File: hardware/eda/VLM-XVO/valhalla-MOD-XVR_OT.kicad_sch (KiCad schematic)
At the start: 35 parts, among them J1 OT+_Boiler, J2 GPIO, J3 OT+_Thermostat, J4 BUS, Q1 Q_PNP, Q2 Q_PNP, Q3 Q_PNP, Q4 Q_PNP, Q5 Q_NPN, Q6 Q_NPN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

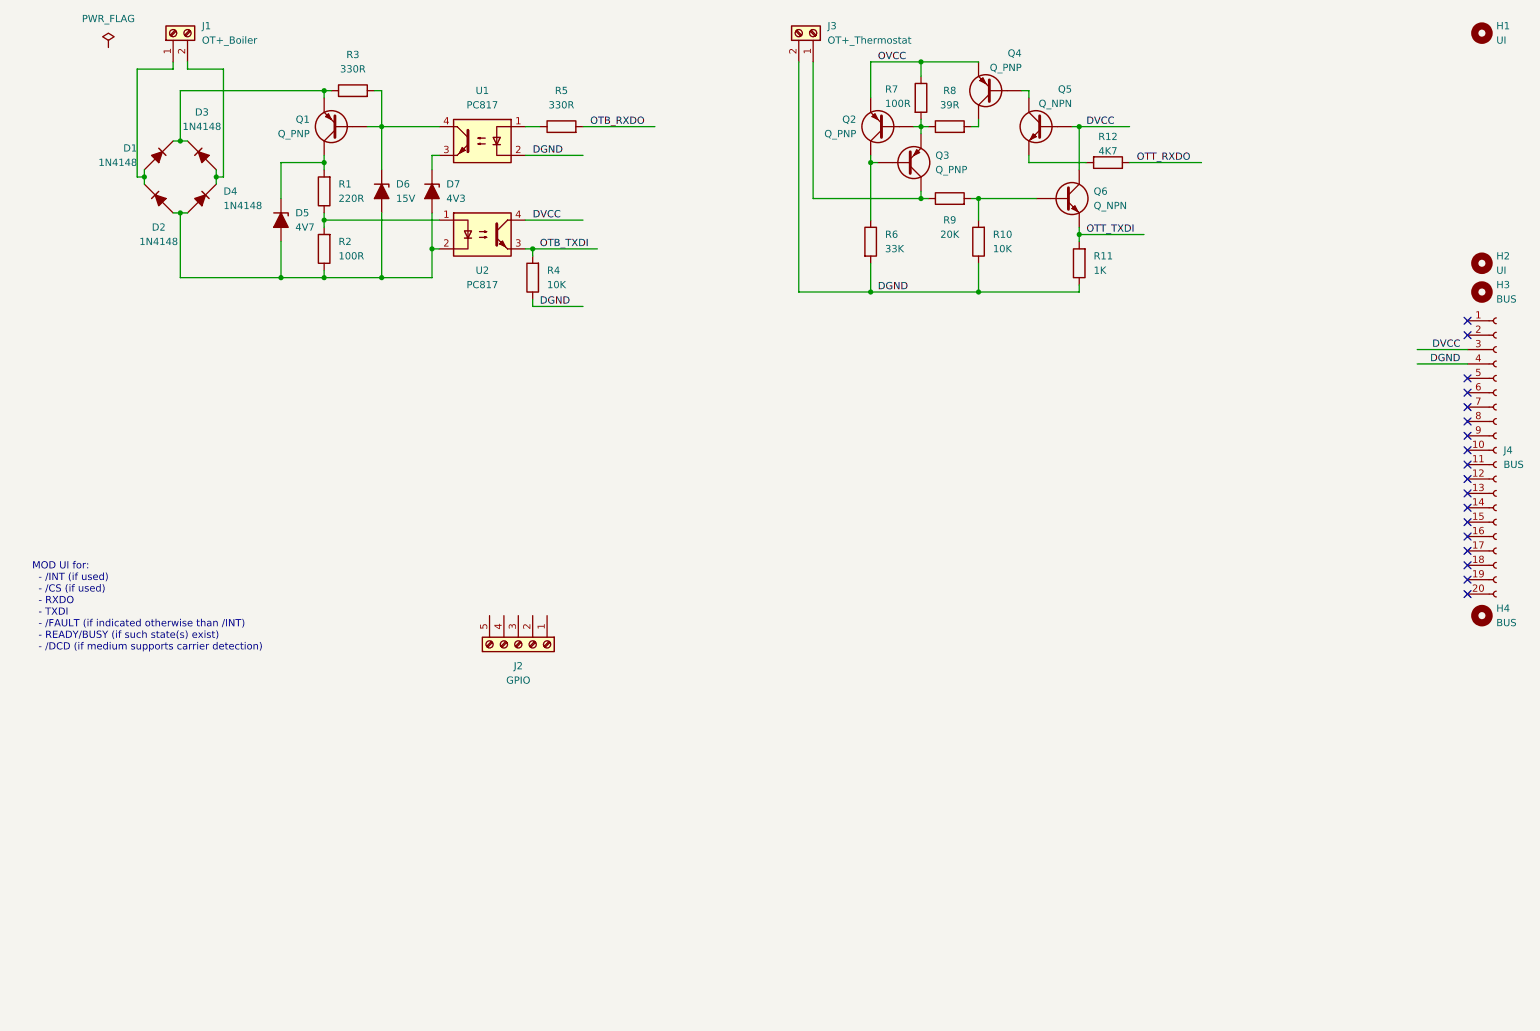
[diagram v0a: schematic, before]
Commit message: UPDATE: progress on MOD-XVR(GPIO-OT-T)
  - added UI LEDs
  - added boost converter socket for 24DC
  - added buffering of boiler-side Tx line
  - still need to add opto-isolation for thermostat side.
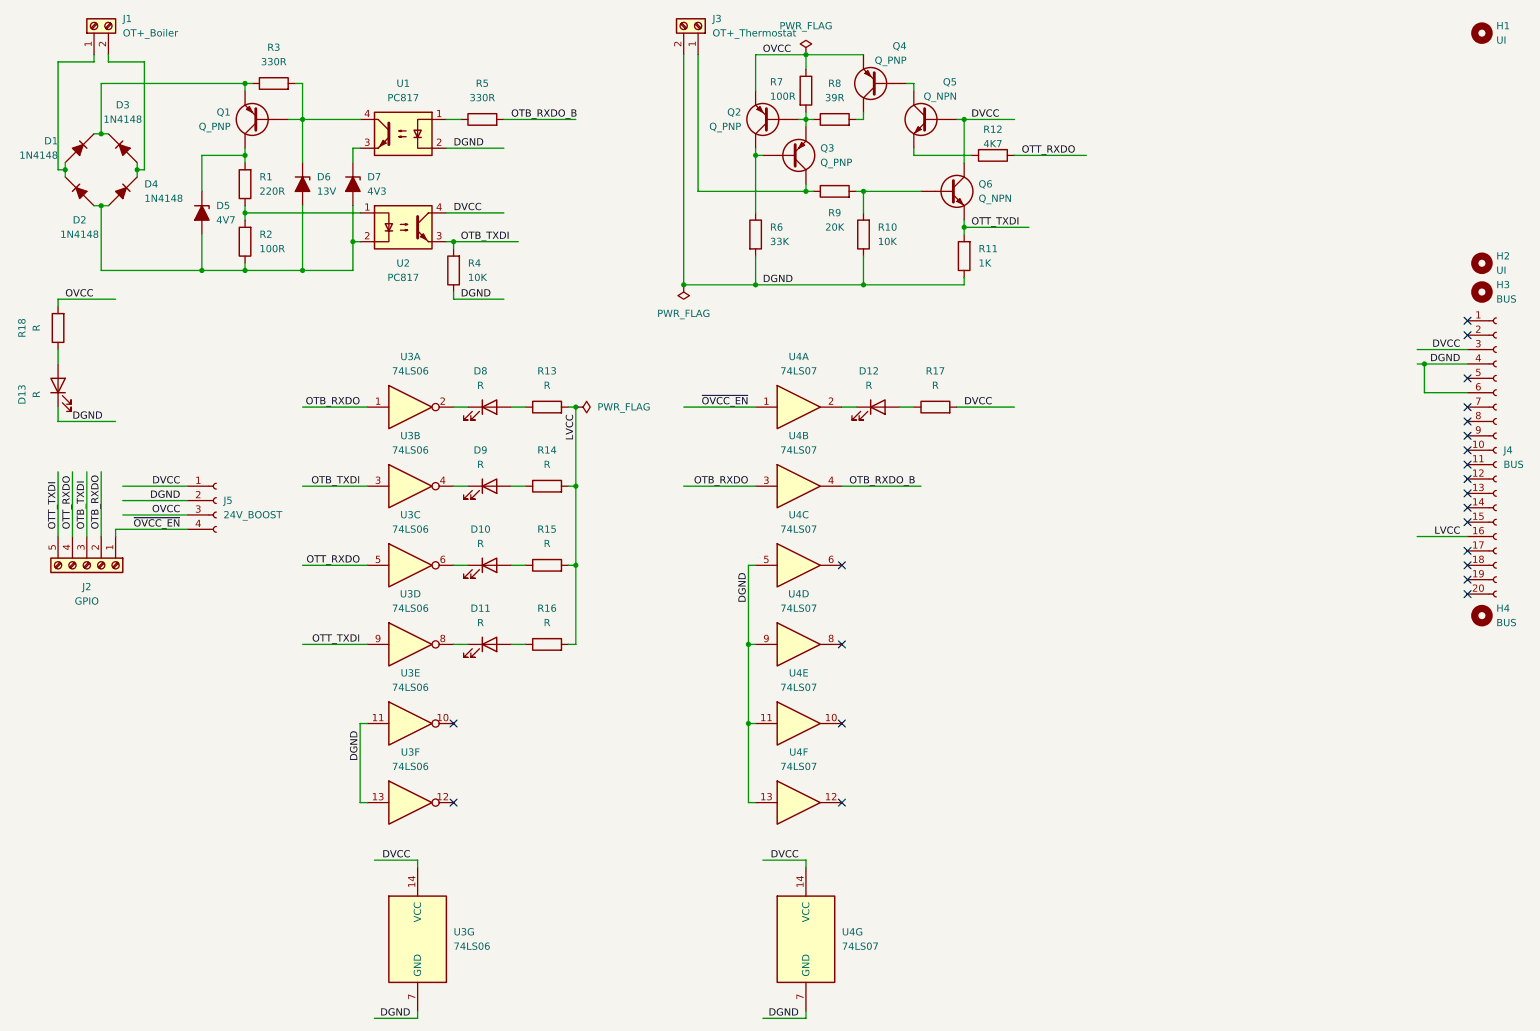
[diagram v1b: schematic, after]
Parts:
- added D10, D11, D12, D13, D8, D9: R, symbol Device:LED
- added J5: 24V_BOOST, Connector_PinSocket_2.54mm:PinSocket_1x04_P2.54mm_Vertical, symbol Connector:Conn_01x04_Socket
- added R13, R14, R15, R16, R17, R18: R, symbol Device:R
- added U3: 74LS06, symbol 74xx:74LS06
- added U4: 74LS07, symbol 74xx:74LS07
- D6: value 15V -> 13V
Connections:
- net DGND: now also J4.6 (Pin_6), D13.1 (K), J5.2 (Pin_2), U3.11, U3.13, U3.7 (GND), U4.11, U4.13, U4.5, U4.7 (GND), U4.9
- net DVCC: now also J5.1 (Pin_1), R17.2, U3.14 (VCC), U4.14 (VCC)
- net OTB_RXDO: now also J2.2 (Pin_2), U3.1, U4.3; no longer R5.2
- net OTB_TXDI: now also J2.3 (Pin_3), U3.3
- net OTT_RXDO: now also J2.4 (Pin_4), U3.5
- net OTT_TXDI: now also J2.5 (Pin_5), U3.9
- net OVCC: now also J5.3 (Pin_3), R18.2
- net ~{OVCC_EN}: now reaches J2.1 (Pin_1)
- net ~{OVCC_EN}: now also J5.4 (Pin_4), U4.1
- net LVCC: now reaches J4.16 (Pin_16)
- net LVCC: now also R13.2, R14.2, R15.2, R16.2
- new net: D10.1 (K), U3.6
- new net: D10.2 (A), R15.1
- new net: D9.2 (A), R14.1
- new net: D8.1 (K), U3.2
- new net: D11.1 (K), U3.8
- new net: D11.2 (A), R16.1
- new net: D12.1 (K), U4.2
- new net: D12.2 (A), R17.1
- new net: D9.1 (K), U3.4
- new net: D13.2 (A), R18.1
- new net: D8.2 (A), R13.1
- new net OTB_RXDO_B: R5.2, U4.4
- no-connect marks 18 -> 22
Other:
- note removed: "MOD UI for: - /INT (if used) - /CS (if used) - RXDO - TXDI - /FAULT (if indicated otherwise than /INT) - READY/BUSY (if such state(s) exist) - /DCD (if medium supports carrier detection)"
- title: (none) -> Valhalla MOD-XVR(GPIO-OT-I)
- moved on the sheet: D1, D2, D3, D4, D5, D6, D7, J1, J2, J3, Q1, Q2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

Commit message: UPDATE: progress on XVR(GPIO-OT-I)
  - full opto-isolation on all GPIOs
  - buffering on all GPIOs driving the LED side of the optocouplers
  - began layout work, this is either going to be a tight or a large
    one.
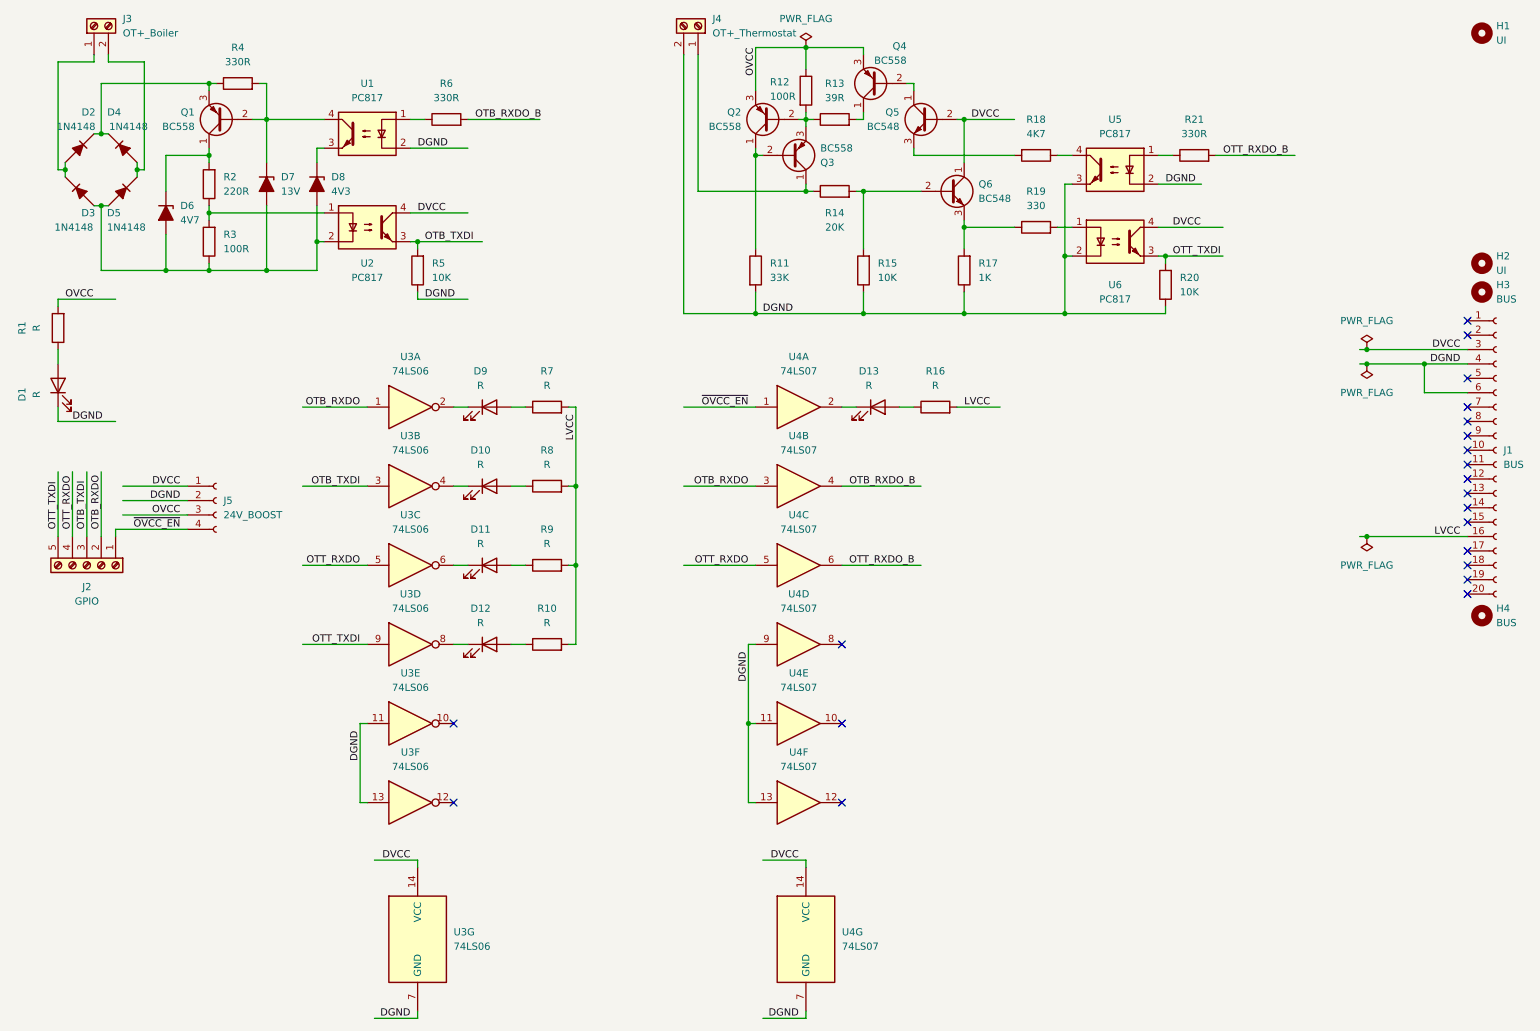
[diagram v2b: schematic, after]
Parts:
- removed Q1, Q2, Q3, Q4: Q_PNP, symbol Device:Q_PNP
- removed Q5, Q6: Q_NPN, symbol Device:Q_NPN
- added Q1, Q2, Q3, Q4: BC558, Package_TO_SOT_THT:TO-92L, symbol Transistor_BJT:BC558
- added Q5, Q6: BC548, Package_TO_SOT_THT:TO-92L, symbol Transistor_BJT:BC548
- added R19: 330, Resistor_THT:R_Axial_DIN0207_L6.3mm_D2.5mm_P5.08mm_Vertical, symbol Device:R
- added R20: 10K, Resistor_THT:R_Axial_DIN0207_L6.3mm_D2.5mm_P5.08mm_Vertical, symbol Device:R
- added R21: 330R, Resistor_THT:R_Axial_DIN0207_L6.3mm_D2.5mm_P5.08mm_Vertical, symbol Device:R
- added U5, U6: PC817, Package_DIP:DIP-4_W7.62mm, symbol Isolator:PC817
- D1: renamed from D13; footprint (none) -> LED_THT:LED_D3.0mm_Horizontal_O1.27mm_Z2.0mm
- D10: renamed from D9; footprint (none) -> LED_THT:LED_D3.0mm_Horizontal_O1.27mm_Z2.0mm
- D11: renamed from D10; footprint (none) -> LED_THT:LED_D3.0mm_Horizontal_O1.27mm_Z2.0mm
- D12: renamed from D11; footprint (none) -> LED_THT:LED_D3.0mm_Horizontal_O1.27mm_Z2.0mm
- D13: renamed from D12; footprint (none) -> LED_THT:LED_D3.0mm_Horizontal_O1.27mm_Z2.0mm
- D2: renamed from D1; footprint (none) -> Diode_THT:D_DO-35_SOD27_P7.62mm_Horizontal
- D3: renamed from D2; footprint (none) -> Diode_THT:D_DO-35_SOD27_P7.62mm_Horizontal
- D4: renamed from D3; footprint (none) -> Diode_THT:D_DO-35_SOD27_P7.62mm_Horizontal
- D5: renamed from D4; footprint (none) -> Diode_THT:D_DO-35_SOD27_P7.62mm_Horizontal
- D6: renamed from D5; footprint (none) -> Diode_THT:D_DO-35_SOD27_P7.62mm_Horizontal
- D7: renamed from D6; footprint (none) -> Diode_THT:D_DO-35_SOD27_P7.62mm_Horizontal
- D8: renamed from D7; footprint (none) -> Diode_THT:D_DO-35_SOD27_P7.62mm_Horizontal
- D9: renamed from D8; footprint (none) -> LED_THT:LED_D3.0mm_Horizontal_O1.27mm_Z2.0mm
- R1: renamed from R18; footprint (none) -> Resistor_THT:R_Axial_DIN0207_L6.3mm_D2.5mm_P5.08mm_Vertical
- R10: renamed from R16; footprint (none) -> Resistor_THT:R_Axial_DIN0207_L6.3mm_D2.5mm_P5.08mm_Vertical
- R11: renamed from R6; footprint (none) -> Resistor_THT:R_Axial_DIN0207_L6.3mm_D2.5mm_P5.08mm_Vertical
- R12: renamed from R7; footprint (none) -> Resistor_THT:R_Axial_DIN0207_L6.3mm_D2.5mm_P5.08mm_Vertical
- R13: renamed from R8; footprint (none) -> Resistor_THT:R_Axial_DIN0207_L6.3mm_D2.5mm_P5.08mm_Vertical
- R14: renamed from R9; footprint (none) -> Resistor_THT:R_Axial_DIN0207_L6.3mm_D2.5mm_P5.08mm_Vertical
- R15: renamed from R10; footprint (none) -> Resistor_THT:R_Axial_DIN0207_L6.3mm_D2.5mm_P5.08mm_Vertical
- R16: renamed from R17; footprint (none) -> Resistor_THT:R_Axial_DIN0207_L6.3mm_D2.5mm_P5.08mm_Vertical
- R17: renamed from R11; footprint (none) -> Resistor_THT:R_Axial_DIN0207_L6.3mm_D2.5mm_P5.08mm_Vertical
- R18: renamed from R12; footprint (none) -> Resistor_THT:R_Axial_DIN0207_L6.3mm_D2.5mm_P5.08mm_Vertical
- R2: renamed from R1; footprint (none) -> Resistor_THT:R_Axial_DIN0207_L6.3mm_D2.5mm_P5.08mm_Vertical
- R3: renamed from R2; footprint (none) -> Resistor_THT:R_Axial_DIN0207_L6.3mm_D2.5mm_P5.08mm_Vertical
- R4: renamed from R3; footprint (none) -> Resistor_THT:R_Axial_DIN0207_L6.3mm_D2.5mm_P5.08mm_Vertical
- R5: renamed from R4; footprint (none) -> Resistor_THT:R_Axial_DIN0207_L6.3mm_D2.5mm_P5.08mm_Vertical
- R6: renamed from R5; footprint (none) -> Resistor_THT:R_Axial_DIN0207_L6.3mm_D2.5mm_P5.08mm_Vertical
- R7: renamed from R13; footprint (none) -> Resistor_THT:R_Axial_DIN0207_L6.3mm_D2.5mm_P5.08mm_Vertical
- R8: renamed from R14; footprint (none) -> Resistor_THT:R_Axial_DIN0207_L6.3mm_D2.5mm_P5.08mm_Vertical
- R9: renamed from R15; footprint (none) -> Resistor_THT:R_Axial_DIN0207_L6.3mm_D2.5mm_P5.08mm_Vertical
- U3, U4: footprint (none) -> Package_DIP:DIP-14_W7.62mm
- renumbered J4 to J1, J1 to J3, J3 to J4
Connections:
- net DGND: now also R20.1, U5.2, U5.3, U6.2; no longer U4.5
- net DVCC: now also Q5.2 (B), Q6.1 (C), U6.4; no longer R16.2
- net LVCC: now also R16.2
- net OTT_RXDO: now also U4.5; no longer R18.1
- net OTT_TXDI: now also R20.2, U6.3; no longer R17.2
- net OVCC: now also Q2.3 (E), Q4.3 (E)
- net at D2.1 (K), D4.1 (K), R4.1: now also Q1.3 (E)
- net at D7.1 (K), R4.2, U1.4: now also Q1.2 (B)
- net at R11.1: now also Q2.1 (C), Q3.2 (B)
- net at R18.2: now also Q5.3 (E)
- net at D6.1 (K), R2.2: now also Q1.1 (C)
- net at R13.2: now also Q4.1 (C)
- net at J4.1 (Pin_1), R14.1: now also Q3.1 (C)
- net at R12.2, R13.1: now also Q2.2 (B), Q3.3 (E)
- net at R14.2, R15.2: now also Q6.2 (B)
- net OTT_RXDO_B: now reaches U4.6
- net OTT_RXDO_B: now also R21.2
- new net: R18.1, U5.4
- new net: R21.1, U5.1
- new net: R19.2, U6.1
- new net: Q6.3 (E), R17.2, R19.1
- new net: Q4.2 (B), Q5.1 (C)
- no-connect marks 22 -> 21
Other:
- moved on the sheet: D6, D7, D8, R11, R15, R17, R18, R2, R3, R4, R5, R6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
